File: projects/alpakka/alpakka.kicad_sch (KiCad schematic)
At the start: 76 parts, among them P1 Debug, P2 Endpoint, P3 Conn_01x02, Q1 Q_PMOS_DGS, U1 Raspberry_Pico, U10 ST_LSM6, U12 ST_LSM6, U2 Alpsalpine_RKJXV, U3 Alpsalpine_EC10E, U4 Alpsalpine_RKJXM, U6 NXP_PCAL6416A, U8 NXP_PCAL6416A

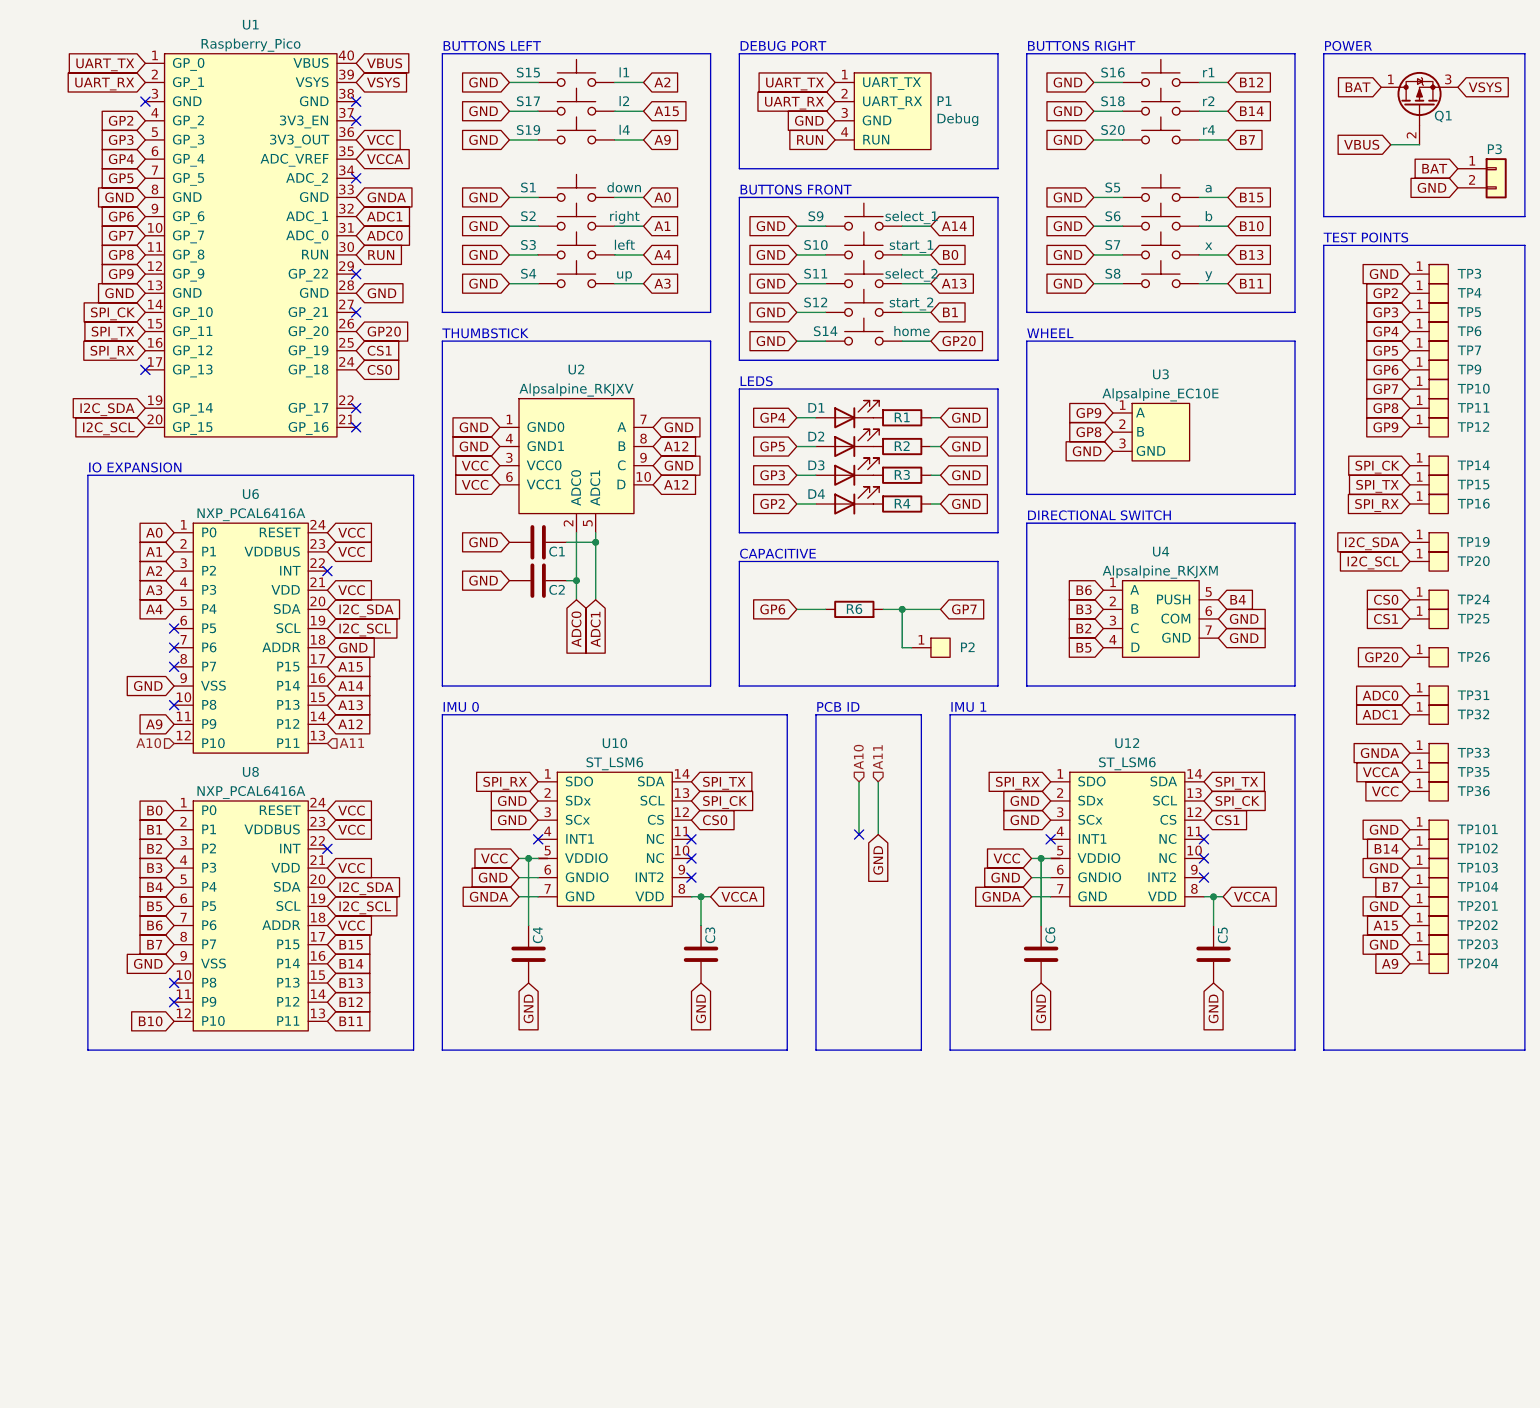
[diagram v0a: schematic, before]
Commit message: Longmao's dual_thumbstick_mod_for_rp2040_picomini
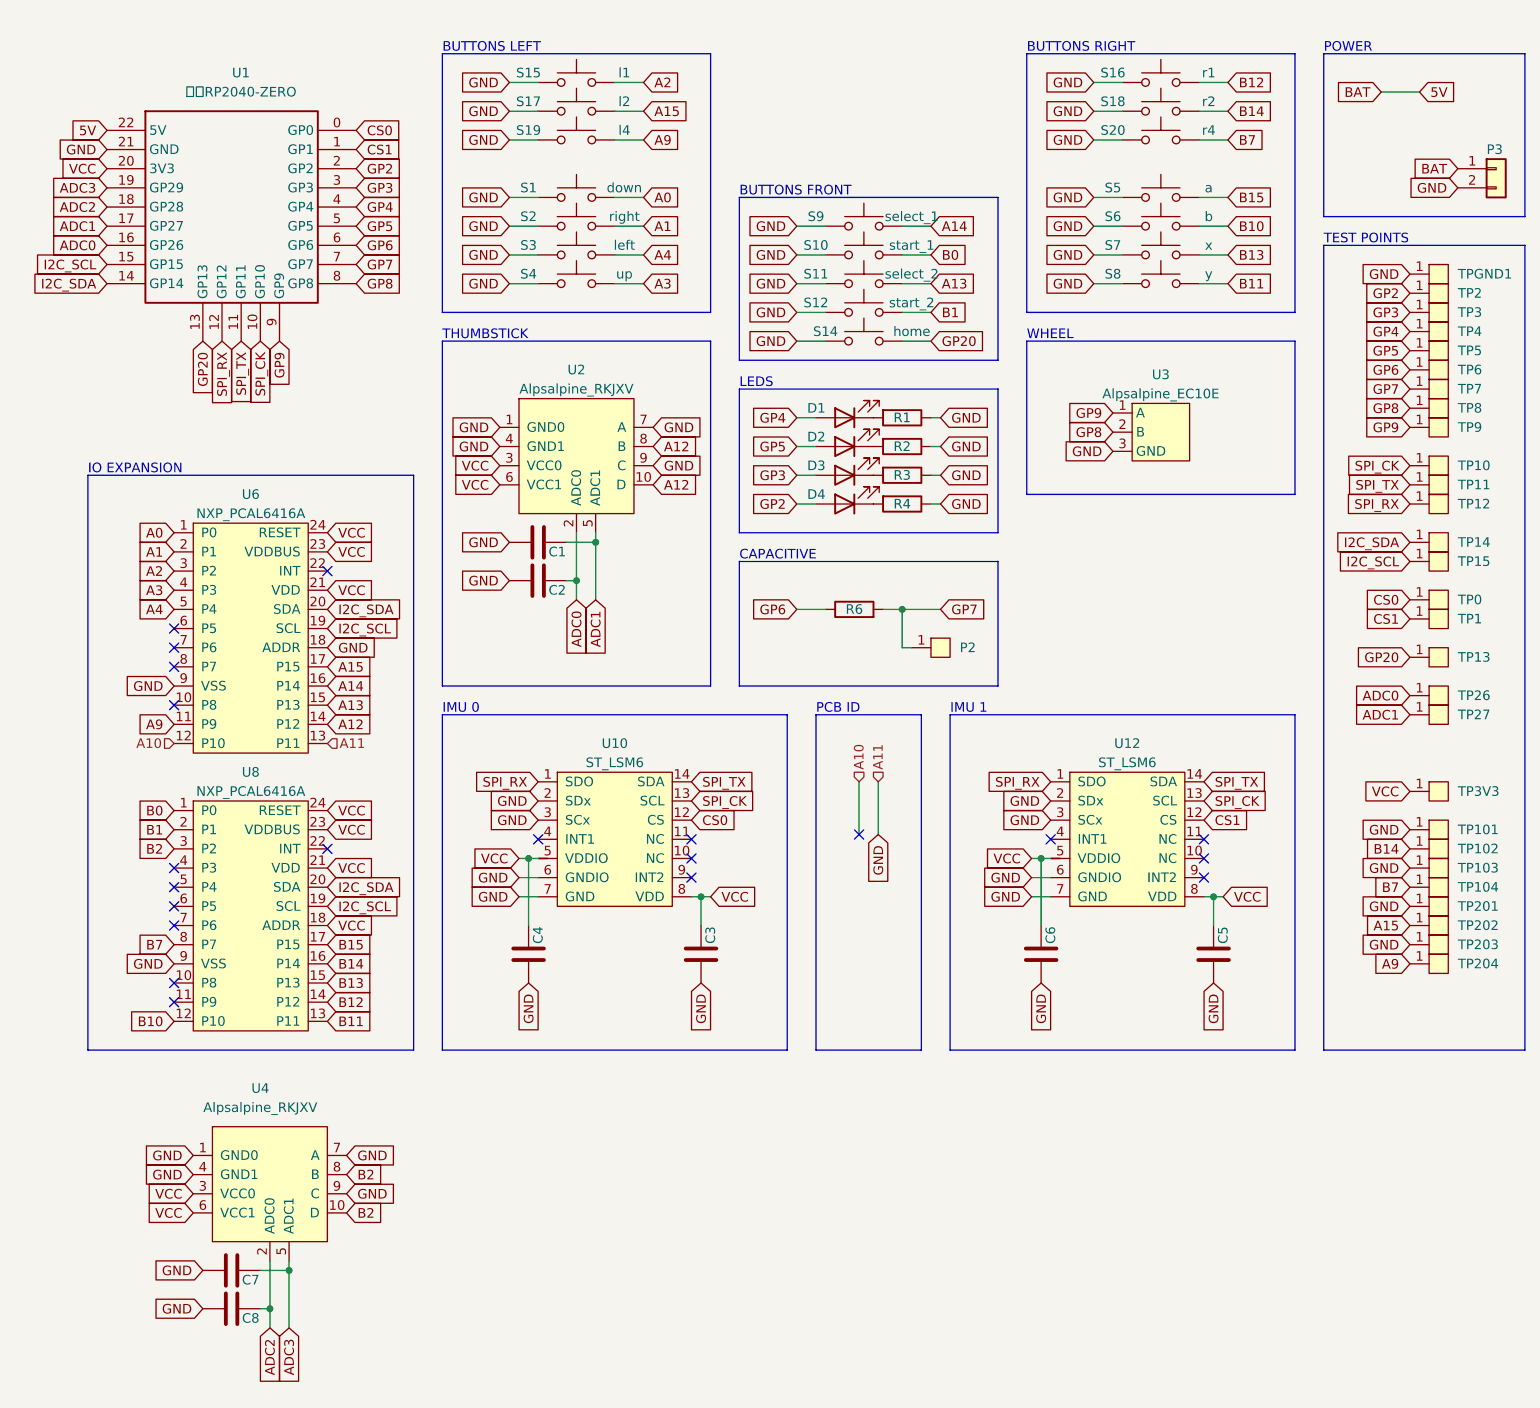
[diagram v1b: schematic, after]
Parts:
- removed P1: Debug, ILO_fp:JST_S4B-PH-SM4-K-TB, symbol ILO_sym:Debug
- removed Q1: Q_PMOS_DGS, ILO_fp:SOT-23-DGS, symbol Device:Q_PMOS_DGS
- removed TP33, TP35: Endpoint, ILO_fp:Pad_1mm, symbol ILO_sym:Endpoint
- removed U1: Raspberry_Pico, ILO_fp:Raspberry_Pico, symbol ILO_sym:Raspberry_Pico
- removed U4: Alpsalpine_RKJXM, ILO_fp:Alpsalpine_RKJXM1015004, symbol ILO_sym:Alpsalpine_RKJXM
- added C7, C8: C, ILO_fp:0402, symbol Device:C
- added U1: 微雪RP2040-ZERO, ILO_fp:PICOMINI, symbol ILO_sym:微雪RP2040-ZERO
- added U4: Alpsalpine_RKJXV, ILO_fp:Alpsalpine_RKJXV122400R, symbol ILO_sym:Alpsalpine_RKJXV
- renumbered TP24 to TP0, TP25 to TP1, TP14 to TP10, TP15 to TP11, TP16 to TP12, TP26 to TP13, TP19 to TP14, TP20 to TP15, TP4 to TP2, TP31 to TP26, TP32 to TP27, TP5 to TP3, TP36 to TP3V3, TP6 to TP4, TP7 to TP5, TP9 to TP6, TP10 to TP7, TP11 to TP8, TP12 to TP9, TP3 to TPGND1
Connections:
- net GNDA is gone; now on net GND: U10.7 (GND), U12.7 (GND)
- net VCCA is gone; now on net VCC: C3.2, C5.2, U10.8 (VDD), U12.8 (VDD)
- net ADC0: now also U1.16 (GP26)
- net ADC1: now also U1.17 (GP27)
- net B2: now also U4.10 (D), U4.8 (B)
- net CS0: now also U1.0 (GP0)
- net CS1: now also U1.1 (GP1)
- net GND: now also C7.1, C8.1, U1.21 (GND), U4.1 (GND0), U4.4 (GND1), U4.7 (A), U4.9 (C)
- net GP2: now also U1.2 (GP2)
- net GP20: now also U1.13 (GP13)
- net GP3: now also U1.3 (GP3)
- net GP4: now also U1.4 (GP4)
- net GP5: now also U1.5 (GP5)
- net GP6: now also U1.6 (GP6)
- net GP7: now also U1.7 (GP7)
- net GP8: now also U1.8 (GP8)
- net GP9: now also U1.9 (GP9)
- net I2C_SCL: now also U1.15 (GP15)
- net I2C_SDA: now also U1.14 (GP14)
- net SPI_CK: now also U1.10 (GP10)
- net SPI_RX: now also U1.12 (GP12)
- net SPI_TX: now also U1.11 (GP11)
- net VCC: now also U1.20 (3V3), U4.3 (VCC0), U4.6 (VCC1)
- net B3: no longer names the net of U8.4 (P3)
- net B4: no longer names the net of U8.5 (P4)
- net B5: no longer names the net of U8.6 (P5)
- net B6: no longer names the net of U8.7 (P6)
- net BAT renamed 5V
- net 5V: now also U1.22 (5V)
- new net ADC2: C8.2, U1.18 (GP28), U4.2 (ADC0)
- new net ADC3: C7.2, U1.19 (GP29), U4.5 (ADC1)
- no-connect marks 26 -> 21
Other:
- note removed: "DEBUG PORT"
- note removed: "DIRECTIONAL SWITCH"
